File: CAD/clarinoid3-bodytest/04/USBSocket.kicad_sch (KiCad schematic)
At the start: 3 parts, among them J5 XKB_U262-16XN-4BVC11 USB-C re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

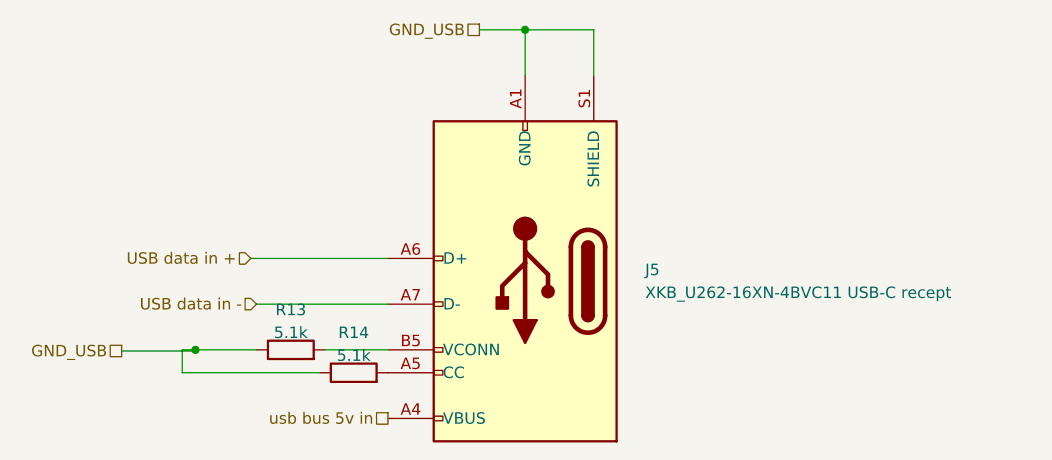
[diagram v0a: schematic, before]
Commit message: c3 design work adding more 3dp tests
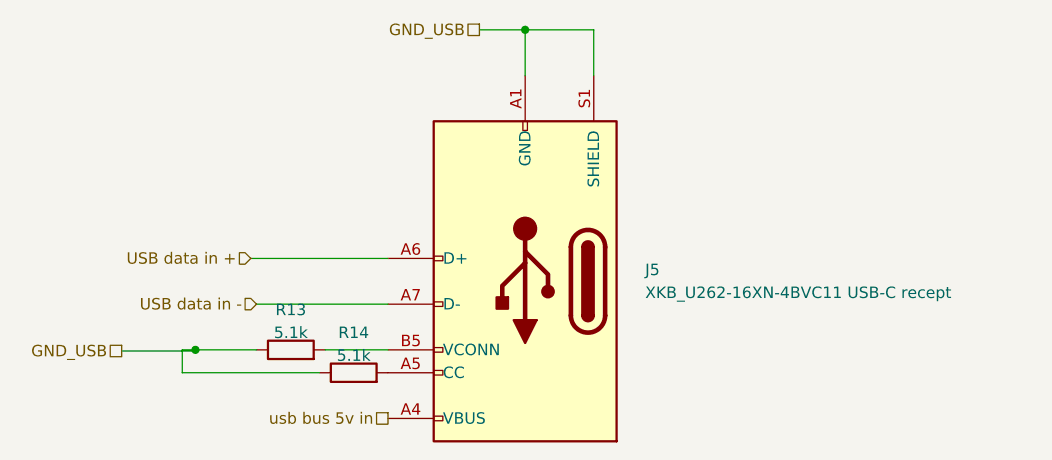
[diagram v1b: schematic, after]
